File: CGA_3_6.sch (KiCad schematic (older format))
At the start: 21 parts, among them U1 74S112, U11 74LS74, U12 74LS393, U13 74LS08, U15 74LS00, U16 74LS04, U17 74LS138, U18 74LS138, U19 74LS138, U26 74S04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

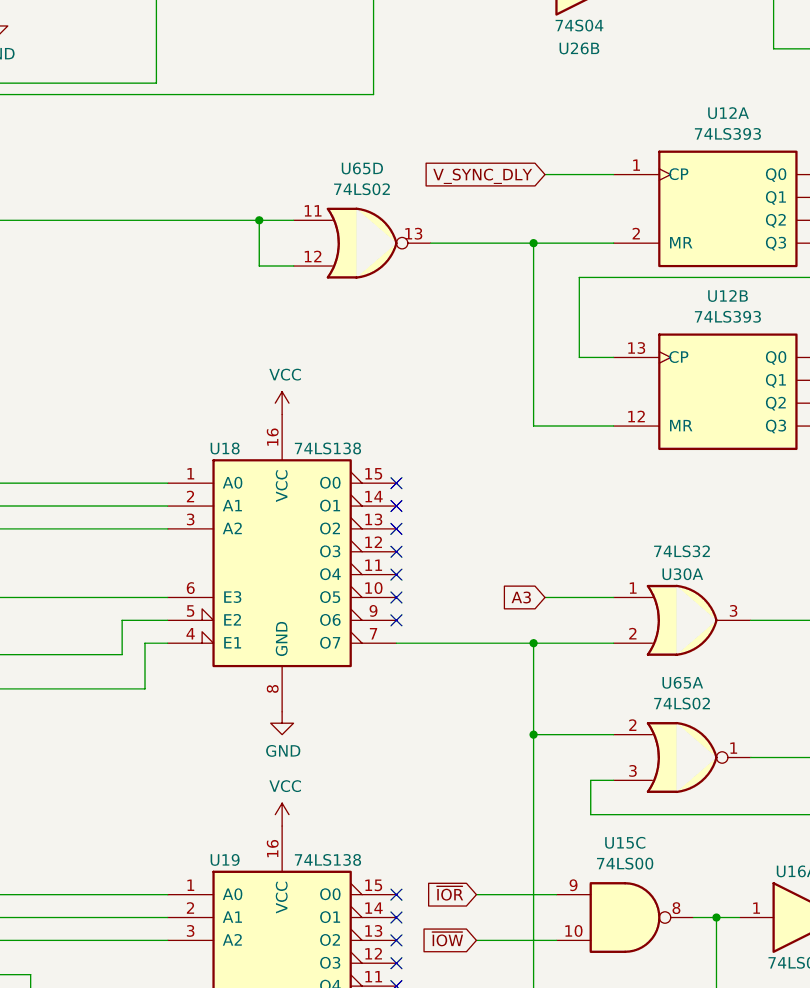
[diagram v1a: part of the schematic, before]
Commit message: Fix some more flags and footprints
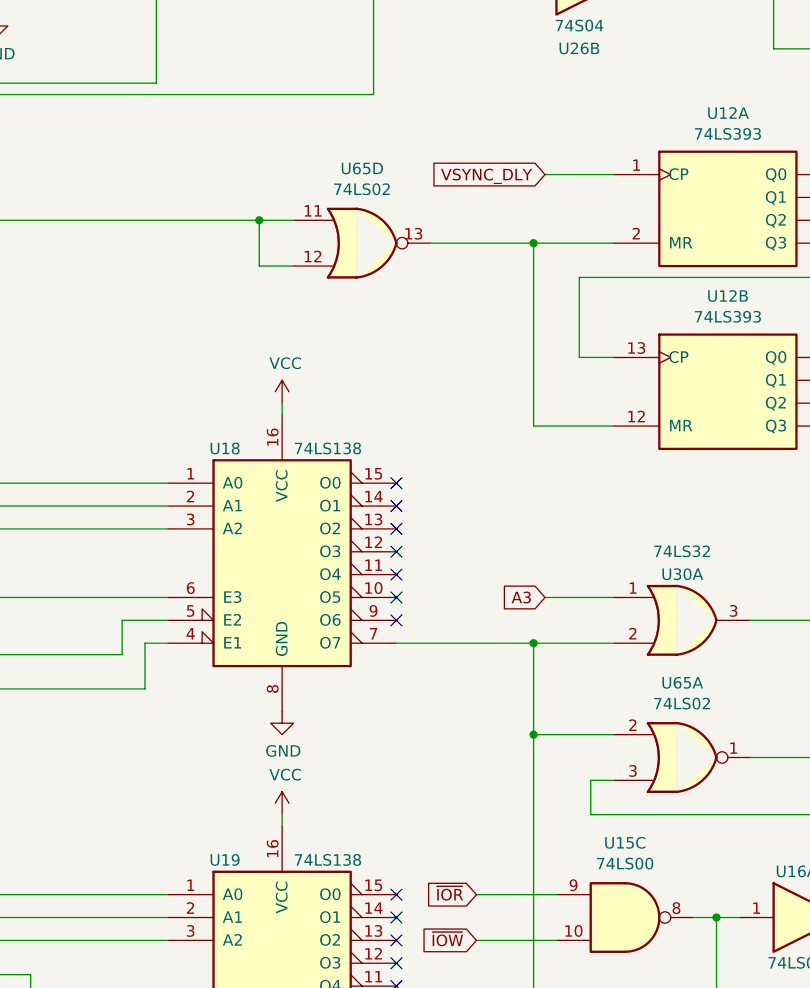
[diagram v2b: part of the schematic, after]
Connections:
- net V_SYNC_DLY renamed VSYNC_DLY
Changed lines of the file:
@@
 Connection ~ 4600 5800
 Text GLabel 4650 5500 0    50   Input ~ 0
-V_SYNC_DLY
+VSYNC_DLY
 Wire Wire Line
 	4650 5500 4950 5500
@@
 L power:VCC #PWR0170
 U 1 1 62178652
-P 3500 6550
-F 0 "#PWR0170" H 3500 6400 50  0001 C CNN
-F 1 "VCC" H 3515 6723 50  0000 C CNN
-F 2 "" H 3500 6550 50  0001 C CNN
-F 3 "" H 3500 6550 50  0001 C CNN
-	1    3500 6550
+P 3500 6500
+F 0 "#PWR0170" H 3500 6350 50  0001 C CNN
+F 1 "VCC" H 3515 6673 50  0000 C CNN
+F 2 "" H 3500 6500 50  0001 C CNN
+F 3 "" H 3500 6500 50  0001 C CNN
+	1    3500 6500
 	1    0    0    -1
 $EndComp
@@
 L power:VCC #PWR0172
 U 1 1 62233746
-P 3500 8350
-F 0 "#PWR0172" H 3500 8200 50  0001 C CNN
-F 1 "VCC" H 3515 8523 50  0000 C CNN
-F 2 "" H 3500 8350 50  0001 C CNN
-F 3 "" H 3500 8350 50  0001 C CNN
-	1    3500 8350
+P 3500 8300
+F 0 "#PWR0172" H 3500 8150 50  0001 C CNN
+F 1 "VCC" H 3515 8473 50  0000 C CNN
+F 2 "" H 3500 8300 50  0001 C CNN
+F 3 "" H 3500 8300 50  0001 C CNN
+	1    3500 8300
 	1    0    0    -1
 $EndComp
@@
 Wire Wire Line
 	5150 2650 5150 3000
+Wire Wire Line
+	3500 8300 3500 8350
+Wire Wire Line
+	3500 6550 3500 6500
 $EndSCHEMATC

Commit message: Changed footprints, moving components
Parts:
- U1, U17, U18, U19, U4, U5: footprint Package_DIP:DIP-16_W7.62mm_LongPads -> Package_DIP:DIP-16_W7.62mm
- U11, U12, U13, U15, U16, U26, U29, U3, U31, U41, U42, U49, U6, U65: footprint Package_DIP:DIP-14_W7.62mm_LongPads -> Package_DIP:DIP-14_W7.62mm
- U30: footprint (none) -> Package_DIP:DIP-14_W7.62mm
